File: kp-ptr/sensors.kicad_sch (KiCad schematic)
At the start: 1 part

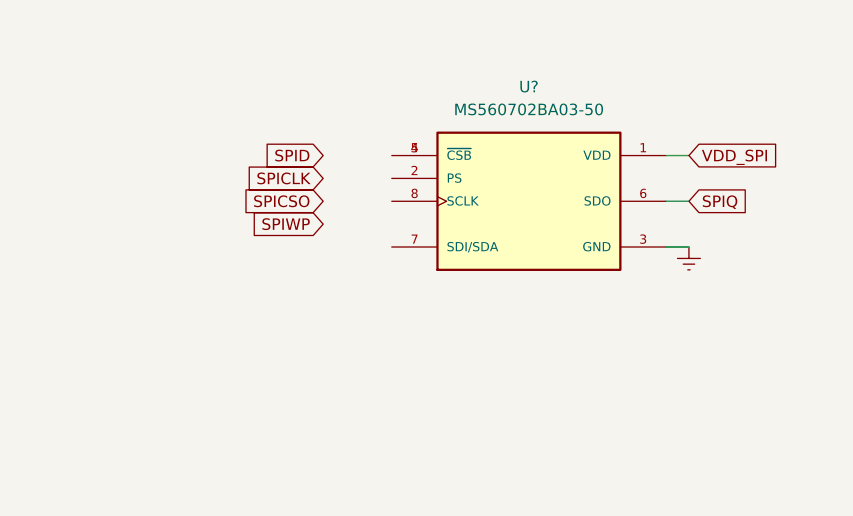
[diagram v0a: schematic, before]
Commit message: Small schematic update
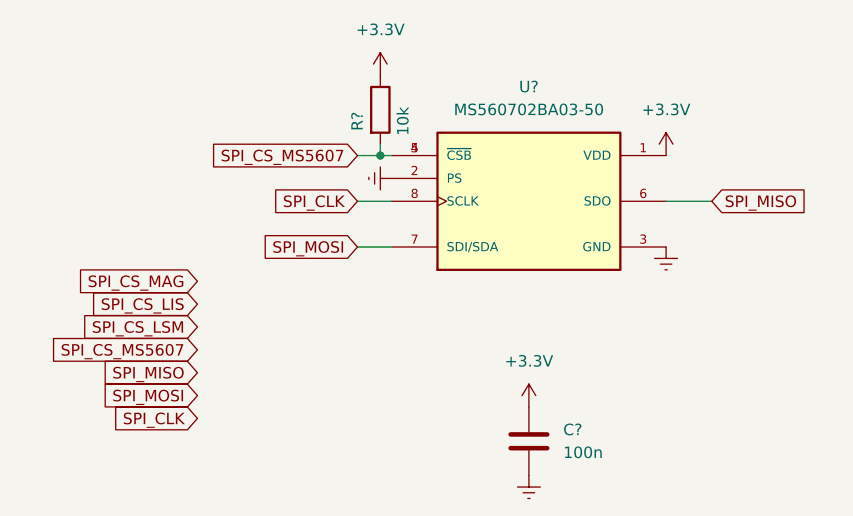
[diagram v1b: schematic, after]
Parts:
- added C?: 100n, symbol Device:C
- added R?: 10k, symbol Device:R
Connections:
- net Earth: now also U?.2 (PS), C?.2
- net SPI_CS_MS5607: now reaches U?.4 (~{CSB}), U?.5 (~{CSB})
- net SPI_CS_MS5607: now also R?.2
- net SPI_MOSI: now reaches U?.7 (SDI/SDA)
- net SPI_CLK: now reaches U?.8 (SCLK)
- net SPIQ renamed SPI_MISO
- net VDD_SPI renamed +3V3
- net +3V3: now also C?.1, R?.1

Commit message: LIS + SDCARD Signed-off-by: kretu <krecik@gmail.com>
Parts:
- added C?: 10uF, symbol Device:C
- added C?: 100nF, symbol Device:C
- added R?: 10k, symbol Device:R
- added U?: LIS331, LGA-16-3X3, symbol KP-PTR_lib:LIS331
- C?: value 100n -> 100nF
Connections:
- net +3V3: now also C?.1, C?.1, R?.1, U?.1 (VDDIO), U?.14 (VDD), U?.15 (VDDR)
- net Earth: now also C?.2, C?.2, U?.10 (GNDR), U?.12 (GND), U?.13 (GND), U?.16 (GND), U?.5 (GND)
- net SPI_CLK: now also U?.4 (SCL/SPC)
- net SPI_CS_LIS: now also R?.2, U?.8 (CS)
- net SPI_MISO: now also U?.7 (SA0/SDO)
- net SPI_MOSI: now also U?.6 (SDA/SDI)

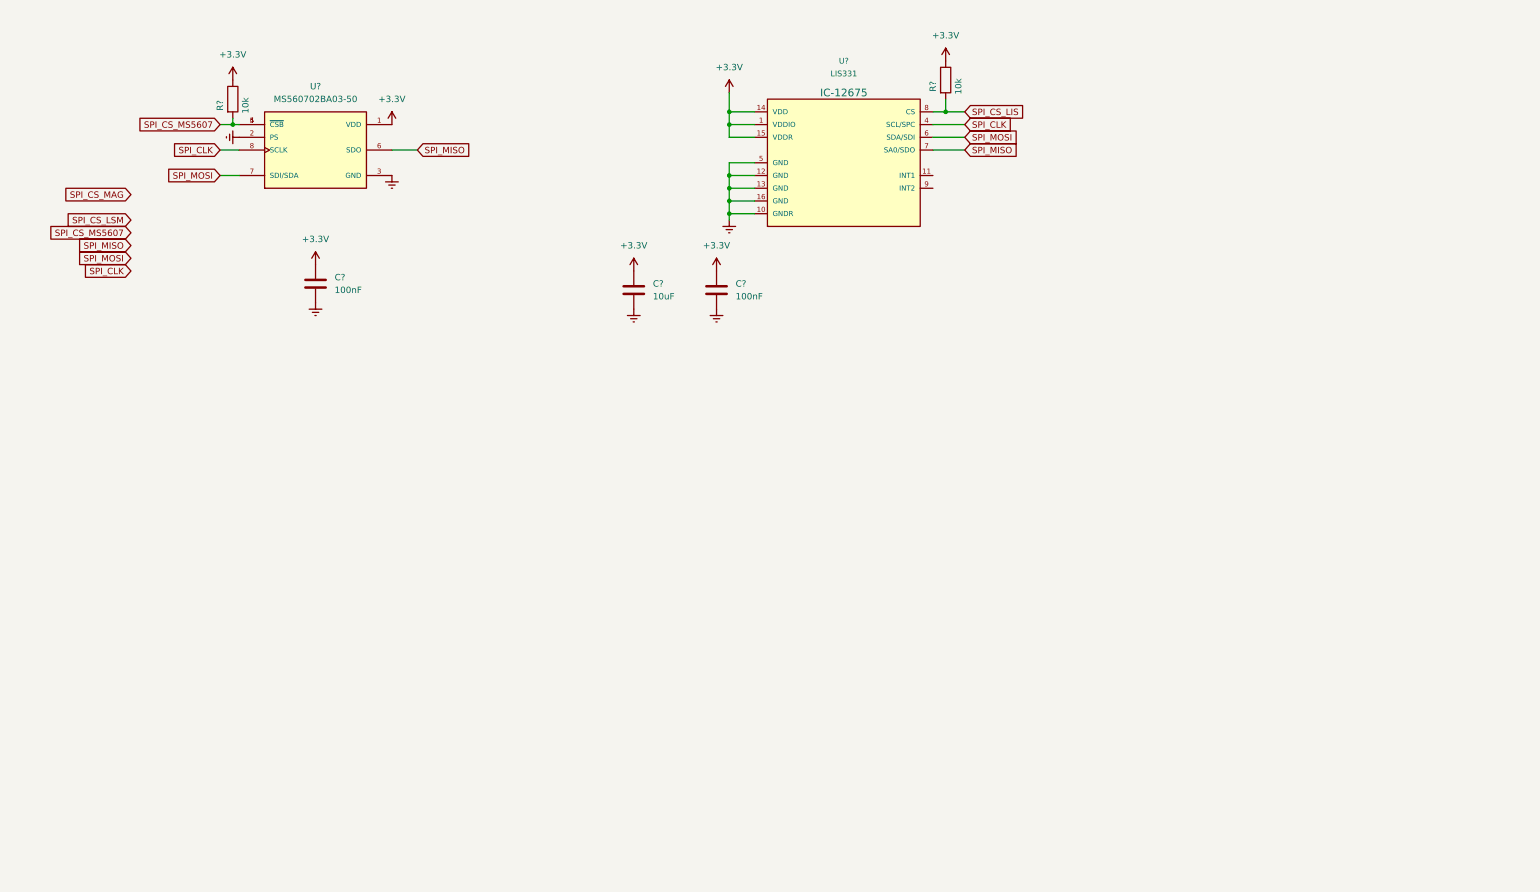
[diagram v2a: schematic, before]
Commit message: Dodane IMU
Signed-off-by: kretu <krecik@gmail.com>
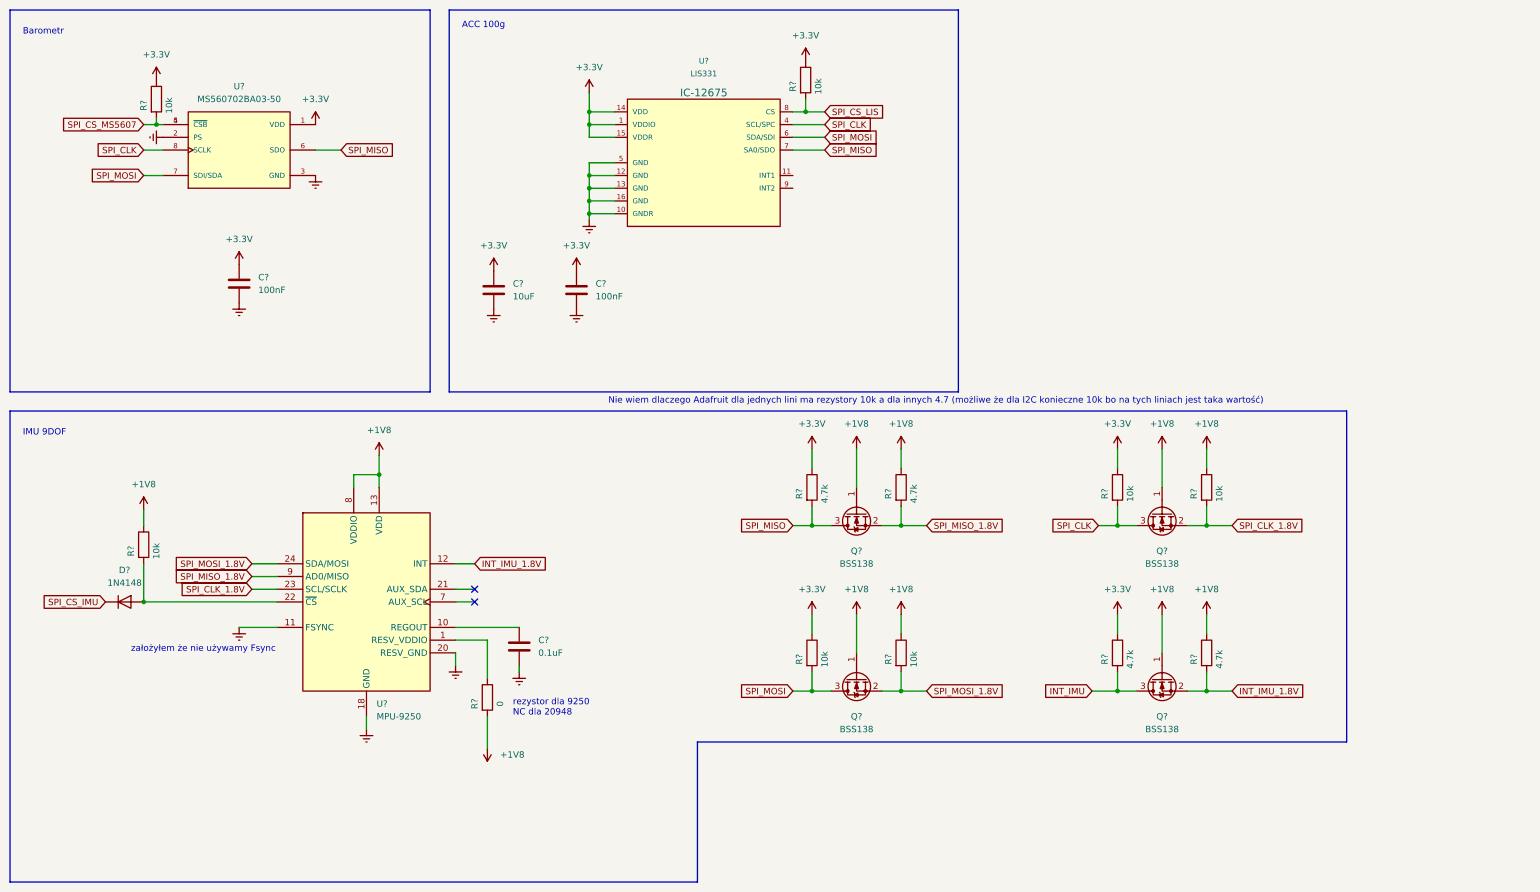
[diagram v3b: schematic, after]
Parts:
- added C?: 0.1uF, symbol Device:C
- added D?: 1N4148, Diode_THT:D_DO-35_SOD27_P7.62mm_Horizontal, symbol Diode:1N4148
- added Q? (x4): BSS138, Package_TO_SOT_SMD:SOT-23, symbol Transistor_FET:BSS138
- added R? (x4): 4.7k, symbol Device:R
- added R? (x5): 10k, symbol Device:R
- added R?: 0, symbol Device:R
- added U?: MPU-9250, Sensor_Motion:InvenSense_QFN-24_3x3mm_P0.4mm, symbol Sensor_Motion:MPU-9250
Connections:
- net +3V3: now also R?.1, R?.1, R?.1, R?.1
- net Earth: now also C?.2, U?.11 (FSYNC), U?.18 (GND), U?.20 (RESV_GND)
- net SPI_CLK: now also Q?.3 (D), R?.2
- net SPI_MISO: now also Q?.3 (D), R?.2
- net SPI_MOSI: now also Q?.3 (D), R?.2
- new net: R?.1, U?.1 (RESV_VDDIO)
- new net: C?.1, U?.10 (REGOUT)
- new net: D?.2 (A), R?.2, U?.22 (~{CS})
- new net +1V8: Q?.1 (G), Q?.1 (G), Q?.1 (G), Q?.1 (G), R?.1, R?.1, R?.1, R?.1, R?.1, R?.2, U?.13 (VDD), U?.8 (VDDIO)
- new net INT_IMU: Q?.3 (D), R?.2
- new net INT_IMU_1.8V: Q?.2 (S), R?.2, U?.12 (INT)
- new net SPI_CLK_1.8V: Q?.2 (S), R?.2, U?.23 (SCL/SCLK)
- new net SPI_CS_IMU: D?.1 (K)
- new net SPI_MISO_1.8V: Q?.2 (S), R?.2, U?.9 (AD0/MISO)
- new net SPI_MOSI_1.8V: Q?.2 (S), R?.2, U?.24 (SDA/MOSI)
- no-connect marks 0 -> 2
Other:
- note added: "ACC 100g"
- note added: "Barometr"
- note added: "IMU 9DOF"
- note added: "Nie wiem dlaczego Adafruit dla jednych lini ma rezystory 10k a dla innych 4.7 (możliwe że dla I2C konieczne 10k bo na tych liniach jest taka wartość)"
- note added: "rezystor dla 9250 NC dla 20948"
- note added: "założyłem że nie używamy Fsync"
- moved on the sheet: C?, R?, U?

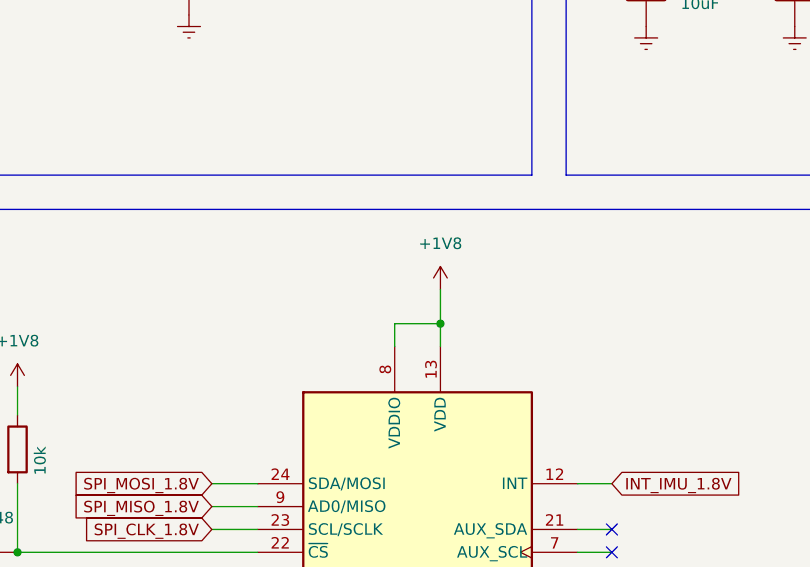
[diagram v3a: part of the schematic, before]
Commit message: Kondensatory przy IMU zgodnie z DS których nie było u Adafruit
Signed-off-by: kretu <krecik@gmail.com>
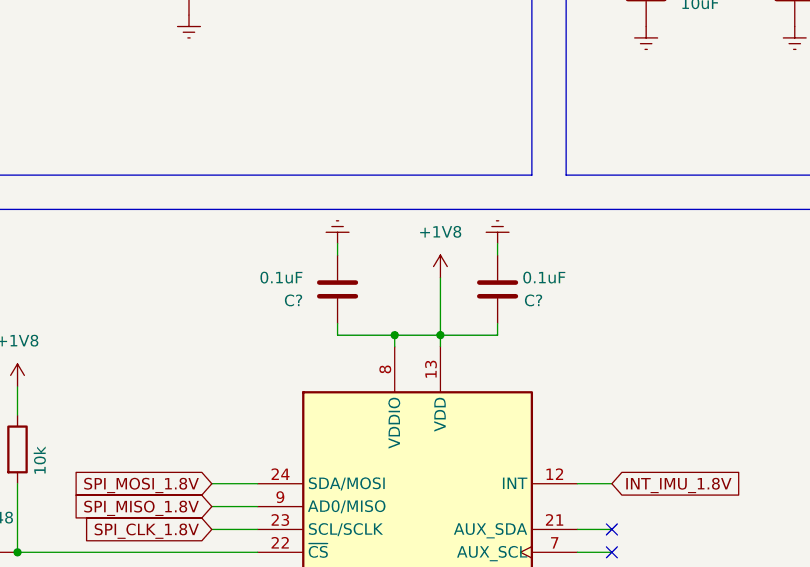
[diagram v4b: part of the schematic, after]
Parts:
- added C? (x2): 0.1uF, symbol Device:C
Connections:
- net +1V8: now also C?.1, C?.1
- net Earth: now also C?.2, C?.2
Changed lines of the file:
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@@
   (junction (at 193.04 121.92) (diameter 0) (color 0 0 0 0)
   )
+  (junction (at 83.82 113.03) (diameter 0) (color 0 0 0 0)
+  )
   (junction (at 41.91 137.16) (diameter 0) (color 0 0 0 0)
   )
@@
   (junction (at 44.45 41.91) (diameter 0) (color 0 0 0 0)
   )
+  (junction (at 88.9 113.03) (diameter 0) (color 0 0 0 0)
+  )
   (junction (at 130.81 41.91) (diameter 0) (color 0 0 0 0)
   )
   (junction (at 130.81 54.61) (diameter 0) (color 0 0 0 0)
-  )
-  (junction (at 88.9 111.76) (diameter 0) (color 0 0 0 0)
   )
   (no_connect (at 107.95 137.16))
@@
     (stroke (width 0) (type default) (color 0 0 0 0))
   )
-  (wire (pts (xy 83.82 114.3) (xy 83.82 111.76))
-    (stroke (width 0) (type default) (color 0 0 0 0))
-  )
   (wire (pts (xy 236.22 121.92) (xy 240.03 121.92))
     (stroke (width 0) (type default) (color 0 0 0 0))
@@
     (stroke (width 0) (type default) (color 0 0 0 0))
   )
+  (wire (pts (xy 83.82 113.03) (xy 88.9 113.03))
+    (stroke (width 0) (type default) (color 0 0 0 0))
+  )
   (wire (pts (xy 231.14 154.94) (xy 236.22 154.94))
     (stroke (width 0) (type default) (color 0 0 0 0))
@@
     (stroke (width 0) (type default) (color 0 0 0 0))
   )
-  (wire (pts (xy 88.9 111.76) (xy 88.9 114.3))
-    (stroke (width 0) (type default) (color 0 0 0 0))
-  )
   (polyline (pts (xy 102.87 95.25) (xy 102.87 19.05))
     (stroke (width 0) (type default) (color 0 0 0 0))
   )
+  (wire (pts (xy 77.47 111.76) (xy 77.47 113.03))
+    (stroke (width 0) (type default) (color 0 0 0 0))
+  )
   (wire (pts (xy 135.89 49.53) (xy 130.81 49.53))
     (stroke (width 0) (type default) (color 0 0 0 0))
@@
     (stroke (width 0) (type default) (color 0 0 0 0))
   )
-  (wire (pts (xy 88.9 107.95) (xy 88.9 111.76))
+  (wire (pts (xy 88.9 106.68) (xy 88.9 113.03))
     (stroke (width 0) (type default) (color 0 0 0 0))
   )
@@
     (stroke (width 0) (type default) (color 0 0 0 0))
   )
+  (wire (pts (xy 88.9 113.03) (xy 88.9 114.3))
+    (stroke (width 0) (type default) (color 0 0 0 0))
+  )
   (wire (pts (xy 41.91 137.16) (xy 41.91 129.54))
     (stroke (width 0) (type default) (color 0 0 0 0))
@@
     (stroke (width 0) (type default) (color 0 0 0 0))
   )
+  (wire (pts (xy 95.25 102.87) (xy 95.25 104.14))
+    (stroke (width 0) (type default) (color 0 0 0 0))
+  )
   (polyline (pts (xy 152.4 193.04) (xy 15.24 193.04))
     (stroke (width 0) (type default) (color 0 0 0 0))
@@
     (stroke (width 0) (type default) (color 0 0 0 0))
   )
+  (wire (pts (xy 83.82 113.03) (xy 83.82 114.3))
+    (stroke (width 0) (type default) (color 0 0 0 0))
+  )
   (wire (pts (xy 130.81 59.69) (xy 130.81 60.96))
     (stroke (width 0) (type default) (color 0 0 0 0))
@@
     (stroke (width 0) (type default) (color 0 0 0 0))
   )
+  (wire (pts (xy 95.25 111.76) (xy 95.25 113.03))
+    (stroke (width 0) (type default) (color 0 0 0 0))
+  )
   (wire (pts (xy 193.04 121.92) (xy 198.12 121.92))
     (stroke (width 0) (type default) (color 0 0 0 0))
@@
     (stroke (width 0) (type default) (color 0 0 0 0))
   )
+  (wire (pts (xy 77.47 113.03) (xy 83.82 113.03))
+    (stroke (width 0) (type default) (color 0 0 0 0))
+  )
   (wire (pts (xy 193.04 151.13) (xy 193.04 154.94))
     (stroke (width 0) (type default) (color 0 0 0 0))
@@
     (stroke (width 0) (type default) (color 0 0 0 0))
   )
+  (wire (pts (xy 77.47 102.87) (xy 77.47 104.14))
+    (stroke (width 0) (type default) (color 0 0 0 0))
+  )
   (wire (pts (xy 175.26 121.92) (xy 179.07 121.92))
     (stroke (width 0) (type default) (color 0 0 0 0))
@@
     (stroke (width 0) (type default) (color 0 0 0 0))
   )
-  (wire (pts (xy 83.82 111.76) (xy 88.9 111.76))
-    (stroke (width 0) (type default) (color 0 0 0 0))
-  )
   (wire (pts (xy 130.81 59.69) (xy 135.89 59.69))
     (stroke (width 0) (type default) (color 0 0 0 0))
   )
   (wire (pts (xy 107.95 137.16) (xy 104.14 137.16))
+    (stroke (width 0) (type default) (color 0 0 0 0))
+  )
+  (wire (pts (xy 95.25 113.03) (xy 88.9 113.03))
     (stroke (width 0) (type default) (color 0 0 0 0))
   )
@@
     )
     (property "Datasheet" "~" (id 3) (at 104.14 149.86 0)
+      (effects (font (size 1.27 1.27)) hide)
+    )
+    (pin "1")
+  )
+  (symbol (lib_id "power:Earth") (at 77.47 102.87 180) (unit 1)
+    (in_bom yes) (on_board yes) (fields_autoplaced)
+    (property "Reference" "#PWR?" (id 0) (at 77.47 96.52 0)
+      (effects (font (size 1.27 1.27)) hide)
+    )
+    (property "Value" "Earth" (id 1) (at 77.47 99.06 0)
+      (effects (font (size 1.27 1.27)) hide)
+    )
+    (property "Footprint" "" (id 2) (at 77.47 102.87 0)
+      (effects (font (size 1.27 1.27)) hide)
+    )
+    (property "Datasheet" "~" (id 3) (at 77.47 102.87 0)
       (effects (font (size 1.27 1.27)) hide)
     )
@@
     (pin "2")
   )
+  (symbol (lib_id "Device:C") (at 77.47 107.95 180) (unit 1)
+    (in_bom yes) (on_board yes) (fields_autoplaced)
+    (property "Reference" "C?" (id 0) (at 73.66 109.2201 0)
+      (effects (font (size 1.27 1.27)) (justify left))
+    )
+    (property "Value" "0.1uF" (id 1) (at 73.66 106.6801 0)
+      (effects (font (size 1.27 1.27)) (justify left))
+    )
+    (property "Footprint" "" (id 2) (at 76.5048 104.14 0)
+      (effects (font (size 1.27 1.27)) hide)
+    )
+    (property "Datasheet" "~" (id 3) (at 77.47 107.95 0)
+      (effects (font (size 1.27 1.27)) hide)
+    )
+    (pin "1")
+    (pin "2")
+  )
   (symbol (lib_id "Device:R") (at 254 147.32 0) (unit 1)
     (in_bom yes) (on_board yes)
@@
     (pin "3")
   )
+  (symbol (lib_id "Device:C") (at 95.25 107.95 180) (unit 1)
+    (in_bom yes) (on_board yes)
+    (property "Reference" "C?" (id 0) (at 100.33 109.22 0)
+      (effects (font (size 1.27 1.27)) (justify left))
+    )
+    (property "Value" "0.1uF" (id 1) (at 102.87 106.68 0)
+      (effects (font (size 1.27 1.27)) (justify left))
+    )
+    (property "Footprint" "" (id 2) (at 94.2848 104.14 0)
+      (effects (font (size 1.27 1.27)) hide)
+    )
+    (property "Datasheet" "~" (id 3) (at 95.25 107.95 0)
+      (effects (font (size 1.27 1.27)) hide)
+    )
+    (pin "1")
+    (pin "2")
+  )
   (symbol (lib_id "Device:R") (at 254 114.3 0) (unit 1)
     (in_bom yes) (on_board yes)
@@
     (pin "1")
   )
+  (symbol (lib_id "power:Earth") (at 95.25 102.87 180) (unit 1)
+    (in_bom yes) (on_board yes) (fields_autoplaced)
+    (property "Reference" "#PWR?" (id 0) (at 95.25 96.52 0)
+      (effects (font (size 1.27 1.27)) hide)
+    )
+    (property "Value" "Earth" (id 1) (at 95.25 99.06 0)
+      (effects (font (size 1.27 1.27)) hide)
+    )
+    (property "Footprint" "" (id 2) (at 95.25 102.87 0)
+      (effects (font (size 1.27 1.27)) hide)
+    )
+    (property "Datasheet" "~" (id 3) (at 95.25 102.87 0)
+      (effects (font (size 1.27 1.27)) hide)
+    )
+    (pin "1")
+  )
   (symbol (lib_id "power:+3.3V") (at 111.76 71.12 0) (unit 1)
     (in_bom yes) (on_board yes) (fields_autoplaced)
@@
     (pin "1")
   )
-  (symbol (lib_id "power:+1V8") (at 88.9 107.95 0) (unit 1)
-    (in_bom yes) (on_board yes) (fields_autoplaced)
-    (property "Reference" "#PWR?" (id 0) (at 88.9 111.76 0)
-      (effects (font (size 1.27 1.27)) hide)
-    )
-    (property "Value" "+1V8" (id 1) (at 88.9 102.87 0))
-    (property "Footprint" "" (id 2) (at 88.9 107.95 0)
-      (effects (font (size 1.27 1.27)) hide)
-    )
-    (property "Datasheet" "" (id 3) (at 88.9 107.95 0)
-      (effects (font (size 1.27 1.27)) hide)
-    )
+  (symbol (lib_id "power:+1V8") (at 88.9 106.68 0) (unit 1)
+    (in_bom yes) (on_board yes) (fields_autoplaced)
+    (property "Reference" "#PWR?" (id 0) (at 88.9 110.49 0)
+      (effects (font (size 1.27 1.27)) hide)
+    )
+    (property "Value" "+1V8" (id 1) (at 88.9 101.6 0))
+    (property "Footprint" "" (id 2) (at 88.9 106.68 0)
+      (effects (font (size 1.27 1.27)) hide)
+    )
+    (property "Datasheet" "" (id 3) (at 88.9 106.68 0)
+      (effects (font (size 1.27 1.27)) hide)
+    )
